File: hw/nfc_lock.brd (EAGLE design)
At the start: 100 x 80 mm, 30 parts, among them IC1 STM8S003F3, IC3 MCP170312MB, Q1 8MHz, U1 M24SR16-YMN6T/2, U2 IRFML8244TRPBF, U3 IRFML8244TRPBF, U4 2N7002BKW, X1 MINI-USB-32005-301

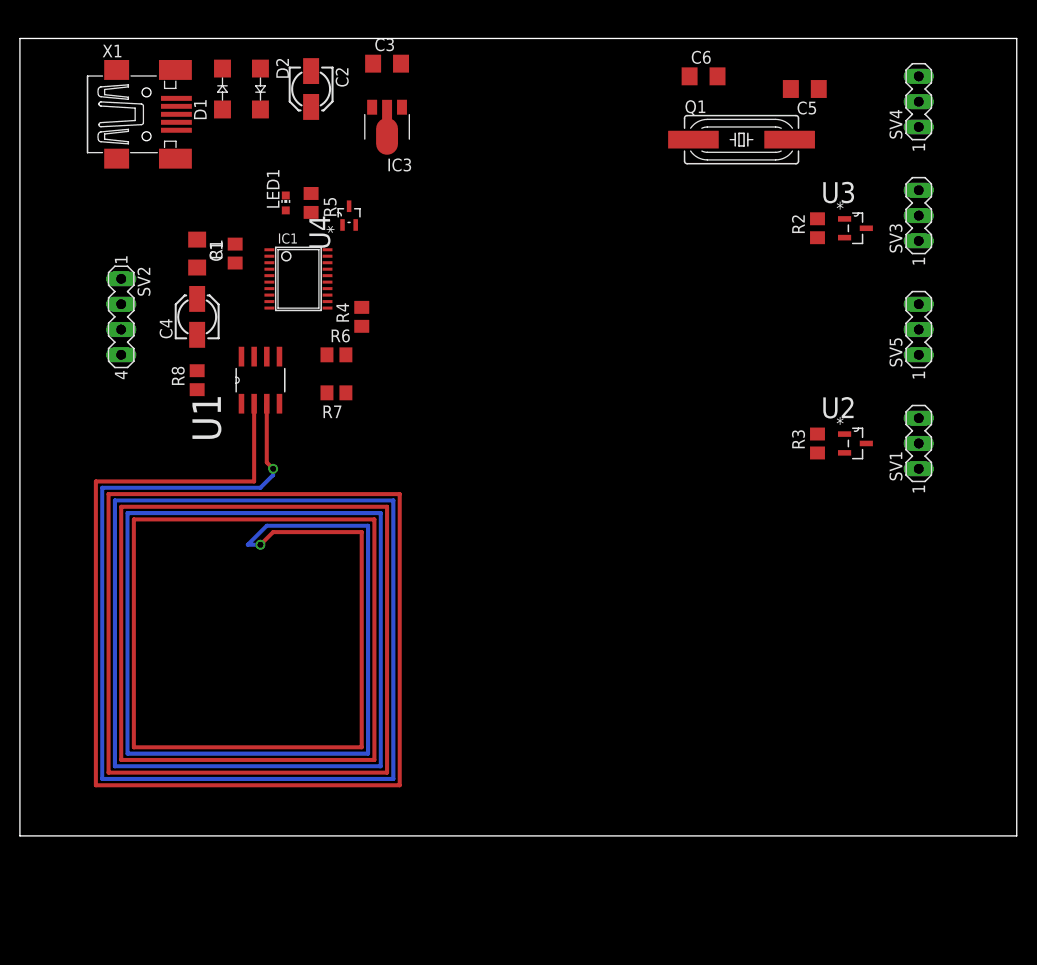
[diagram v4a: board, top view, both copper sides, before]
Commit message: all airewires routed - input for some optimizations
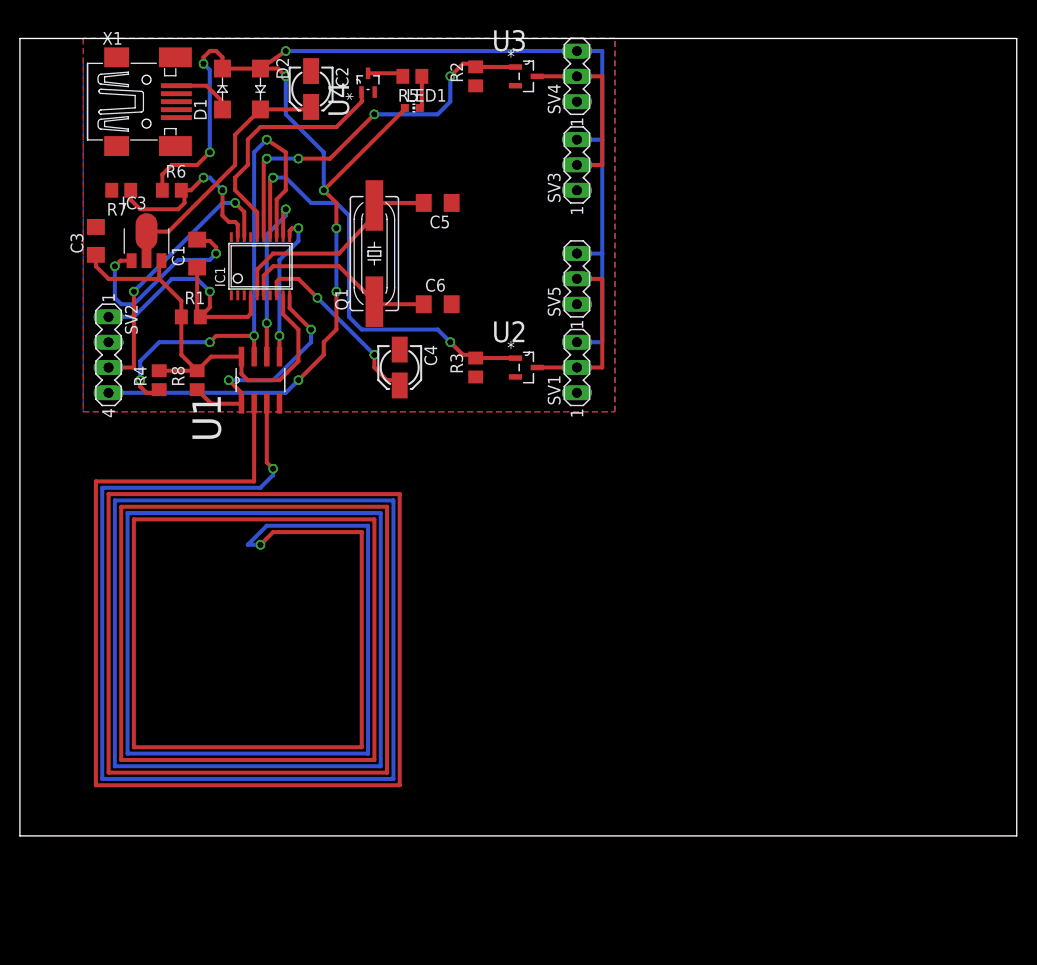
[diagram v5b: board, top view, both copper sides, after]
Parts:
- moved C5 38.6 mm to (41.9, 63.5)
- moved Q1 38.6 mm to (35.6, 58.4), turned to 90 degrees
- moved R2 37.5 mm to (45.7, 76.2)
- moved U3 36.4 mm to (50.8, 76.2)
- moved R3 35.1 mm to (45.7, 47.0)
- moved C6 35.1 mm to (41.9, 53.3)
- moved SV1 35.1 mm to (55.9, 47.0)
- moved SV3 34.7 mm to (55.9, 67.3)
- moved SV5 34.7 mm to (55.9, 55.9)
- moved SV4 34.4 mm to (55.9, 76.2)
- moved C3 34.2 mm to (7.62, 59.7), turned to 90 degrees
- moved U2 33.9 mm to (50.8, 47.0)
- moved R7 29.6 mm to (10.2, 64.8)
- moved IC3 26.7 mm to (12.7, 59.7), turned to 0 degrees
- moved R6 23.3 mm to (15.2, 64.8)
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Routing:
- net +5V/2: track 0.00 -> 164.3 mm, vias 0 -> 8
- net N$8: track 0.00 -> 50.8 mm, vias 0 -> 4
- net +5V/1: track 0.00 -> 45.3 mm
- net N$3: track 0.00 -> 43.9 mm, vias 0 -> 2
- net N$13: track 0.00 -> 38.5 mm, vias 0 -> 4
- net N$6: track 0.00 -> 27.8 mm, vias 0 -> 2
- net N$5: track 0.00 -> 27.5 mm, vias 0 -> 1
- net N$19: track 0.00 -> 25.2 mm
- net N$4: track 0.00 -> 23.5 mm
- net N$7: track 0.00 -> 23.3 mm, vias 0 -> 2
- net N$16: track 0.00 -> 22.7 mm
- net 0V: track 0.00 -> 20.5 mm, vias 0 -> 2
- net N$17: track 0.00 -> 20.0 mm
- net N$18: track 0.00 -> 19.3 mm, vias 0 -> 2
- net N$15: track 0.00 -> 19.0 mm, vias 0 -> 2
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- added copper zone on layer 1, net 0V
- added copper zone on layer 16, net 0V

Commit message: PCB shrinked + board name and revision added
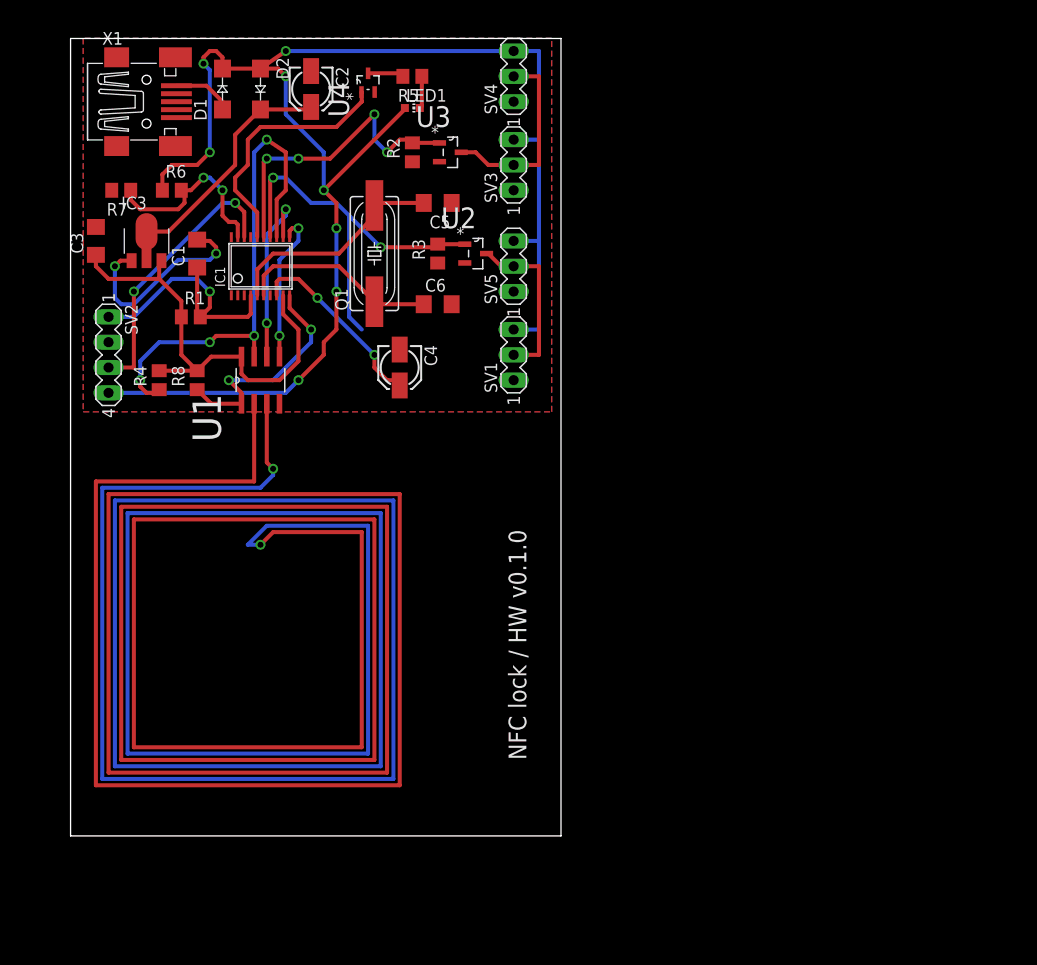
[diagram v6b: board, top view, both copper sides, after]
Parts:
- moved U2 12.5 mm to (45.7, 58.4)
- moved R3 12.0 mm to (41.9, 58.4)
- moved U3 10.8 mm to (43.2, 68.6)
- moved R2 9.92 mm to (39.4, 68.6)
- moved SV1 6.48 mm to (49.5, 48.3)
- moved SV5 6.48 mm to (49.5, 57.1)
- moved SV3 6.35 mm to (49.5, 67.3)
- moved SV4 6.35 mm to (49.5, 76.2)
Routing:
- net +5V/2: track 164.3 -> 156.7 mm
- net N$13: track 38.5 -> 30.9 mm
- net N$3: track 43.9 -> 40.3 mm
- net N$11: track 18.0 -> 19.8 mm
- net N$9: track 18.0 -> 17.2 mm
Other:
- board size 100 x 80 mm -> 49.2 x 80 mm
- board text added: "NFC lock / HW v0.1.0"

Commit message: antenna's surronding space limited
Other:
- board size 49.2 x 80 mm -> 49.2 x 76.2 mm
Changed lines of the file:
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@@
 <board>
 <plain>
-<wire x1="5.08" y1="0" x2="54.28" y2="0" width="0" layer="20"/>
-<wire x1="54.28" y1="0" x2="54.28" y2="80" width="0" layer="20"/>
+<wire x1="5.08" y1="3.81" x2="54.28" y2="3.81" width="0" layer="20"/>
+<wire x1="54.28" y1="3.81" x2="54.28" y2="80" width="0" layer="20"/>
 <wire x1="54.28" y1="80" x2="5.08" y2="80" width="0" layer="20"/>
-<wire x1="5.08" y1="80" x2="5.08" y2="0" width="0" layer="20"/>
-<text x="50.8" y="7.62" size="1.778" layer="25" rot="R90">NFC lock / HW v0.1.0</text>
+<wire x1="5.08" y1="80" x2="5.08" y2="3.81" width="0" layer="20"/>
+<text x="48.26" y="10.16" size="1.778" layer="25" rot="R90">NFC lock / HW v0.1.0</text>
 </plain>
 <attributes>

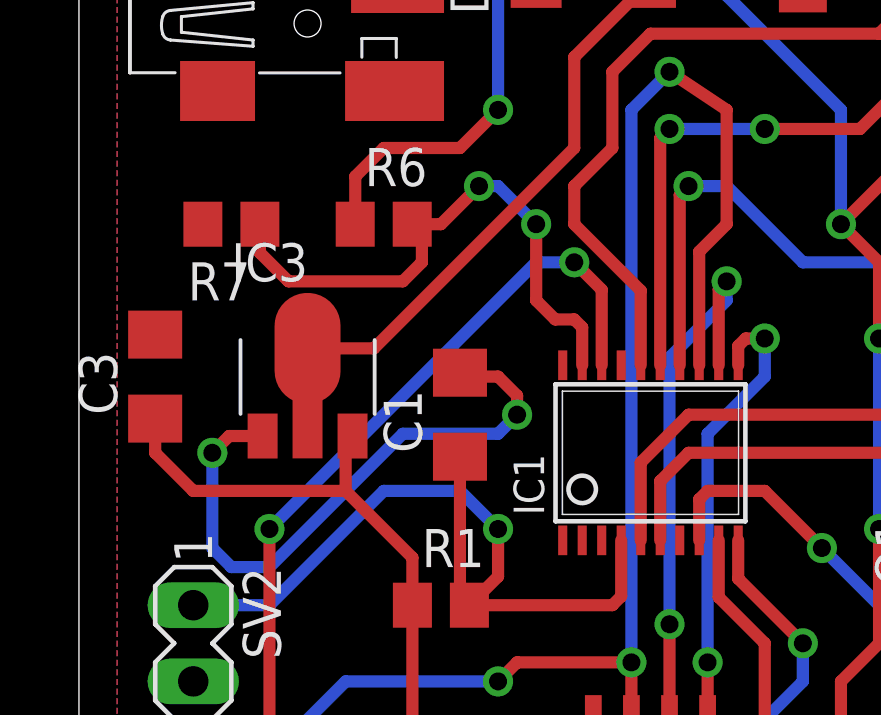
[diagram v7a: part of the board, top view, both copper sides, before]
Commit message: fixed/approved all found warnings and errors
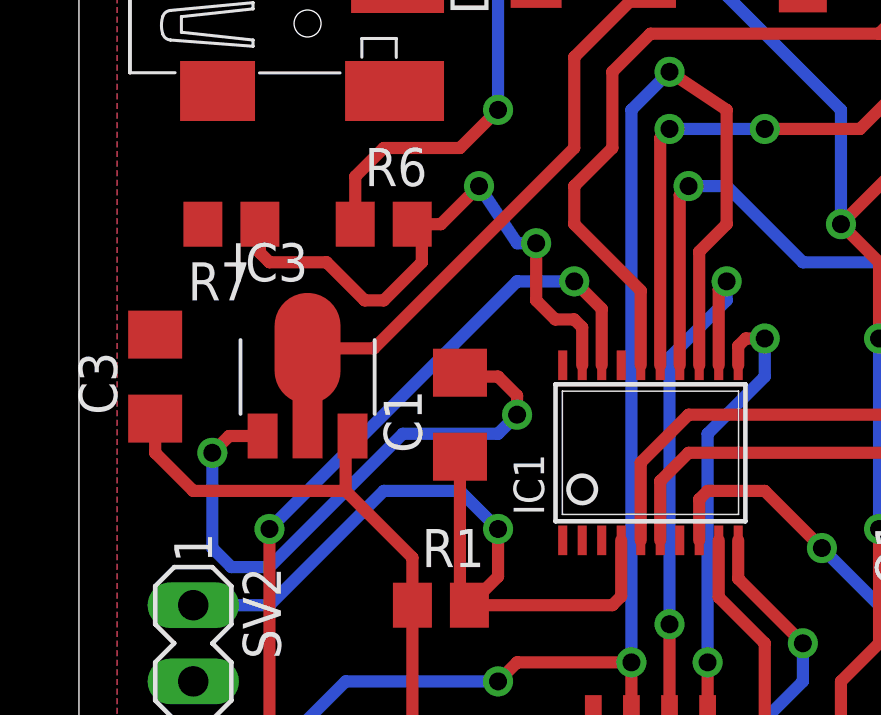
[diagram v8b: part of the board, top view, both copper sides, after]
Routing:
- net N$6: track 27.8 -> 26.9 mm
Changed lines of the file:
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@@
 <contactref element="IC1" pad="18"/>
 <contactref element="SV2" pad="3"/>
-<wire x1="22.505" y1="60.0678" x2="22.505" y2="62.585" width="0.4064" layer="1"/>
-<wire x1="22.505" y1="62.585" x2="21.59" y2="63.5" width="0.4064" layer="1"/>
-<via x="21.59" y="63.5" extent="1-16" drill="0.6"/>
-<wire x1="21.59" y1="63.5" x2="20.32" y2="63.5" width="0.4064" layer="16"/>
-<wire x1="20.32" y1="63.5" x2="11.43" y2="54.61" width="0.4064" layer="16"/>
+<wire x1="22.505" y1="60.0678" x2="22.505" y2="61.95" width="0.4064" layer="1"/>
+<wire x1="22.505" y1="61.95" x2="21.59" y2="62.865" width="0.4064" layer="1"/>
+<via x="21.59" y="62.865" extent="1-16" drill="0.6"/>
+<wire x1="21.59" y1="62.865" x2="19.685" y2="62.865" width="0.4064" layer="16"/>
+<wire x1="19.685" y1="62.865" x2="11.43" y2="54.61" width="0.4064" layer="16"/>
 <via x="11.43" y="54.61" extent="1-16" drill="0.6"/>
 <wire x1="11.43" y1="54.61" x2="11.43" y2="46.99" width="0.4064" layer="1"/>
@@
 <contactref element="R7" pad="1"/>
 <wire x1="11.11" y1="64.77" x2="11.11" y2="63.82" width="0.4064" layer="1"/>
-<wire x1="11.11" y1="63.82" x2="12.065" y2="62.865" width="0.4064" layer="1"/>
-<wire x1="12.065" y1="62.865" x2="15.875" y2="62.865" width="0.4064" layer="1"/>
-<wire x1="15.875" y1="62.865" x2="16.51" y2="63.5" width="0.4064" layer="1"/>
+<wire x1="11.11" y1="63.82" x2="11.43" y2="63.5" width="0.4064" layer="1"/>
+<wire x1="11.43" y1="63.5" x2="13.335" y2="63.5" width="0.4064" layer="1"/>
+<wire x1="13.335" y1="63.5" x2="14.605" y2="62.23" width="0.4064" layer="1"/>
+<wire x1="14.605" y1="62.23" x2="15.24" y2="62.23" width="0.4064" layer="1"/>
+<wire x1="15.24" y1="62.23" x2="16.51" y2="63.5" width="0.4064" layer="1"/>
 <wire x1="16.51" y1="63.5" x2="16.51" y2="64.45" width="0.4064" layer="1"/>
 <wire x1="16.51" y1="64.45" x2="16.19" y2="64.77" width="0.4064" layer="1"/>
@@
 <wire x1="17.145" y1="64.77" x2="18.415" y2="66.04" width="0.4064" layer="1"/>
 <via x="18.415" y="66.04" extent="1-16" drill="0.6"/>
-<wire x1="18.415" y1="66.04" x2="19.05" y2="66.04" width="0.4064" layer="16"/>
-<wire x1="19.05" y1="66.04" x2="20.32" y2="64.77" width="0.4064" layer="16"/>
-<via x="20.32" y="64.77" extent="1-16" drill="0.6"/>
-<wire x1="20.32" y1="64.77" x2="20.32" y2="62.23" width="0.4064" layer="1"/>
+<wire x1="18.415" y1="66.04" x2="19.685" y2="64.135" width="0.4064" layer="16"/>
+<wire x1="19.685" y1="64.135" x2="20.32" y2="64.135" width="0.4064" layer="16"/>
+<via x="20.32" y="64.135" extent="1-16" drill="0.6"/>
+<wire x1="20.32" y1="64.135" x2="20.32" y2="62.23" width="0.4064" layer="1"/>
 <wire x1="21.855" y1="60.0678" x2="21.855" y2="61.33" width="0.4064" layer="1"/>
 <wire x1="21.855" y1="61.33" x2="21.59" y2="61.595" width="0.4064" layer="1"/>
@@
 </signal>
 </signals>
+<errors>
+</errors>
 </board>
 </drawing>
